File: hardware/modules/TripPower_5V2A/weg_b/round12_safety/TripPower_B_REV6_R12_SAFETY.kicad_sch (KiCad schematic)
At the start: 29 parts, among them Q301 MMBT3904LT1G, Q302 BSS138LT1G, Q401 TK11S10N1L,LQ, Q402 TK11S10N1L,LQ, Q403 BSS123LT1G, U301 TPS7A4001DGNR, U302 TMP390AQDRLRQ1, U303 TPS3838K33QDBVRQ1, U401 LTC4368HMS-2#WPBF

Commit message: fix(b): align isolated KiCad net labels and wires to placed component pin coordinates
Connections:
- net BASE_KILL: now also Q302.3 (D)
- net GND: now also U301.4 (GND), U301.9 (EP), U302.3 (GND), U303.2 (GND), U401.4 (RETRY), U401.5 (GND)
- net RAW_COMMON_SOURCE: now also Q401.3 (S), Q402.3 (S)
- net RAW_GATE: now also U401.10 (GATE)
- net RAW_LTC_SHDN: now also Q403.3 (D), U401.6 (SHDN)
- net RAW_OUT: now also U401.8 (VOUT)
- net RAW_OV: now also U401.3 (OV)
- net RAW_SENSE: now also U401.9 (SENSE)
- net RAW_UV: now also U401.2 (UV)
- net SAFE_3V3: now also U302.5 (VDD), U303.3 (MR), U303.5 (VDD)
- net SAFE_HV: now also U301.5 (EN), U301.8 (IN)
- net TEMP_OK_OD: now also U302.6 (OUTA)
- net TEMP_SET: now also U302.2 (SETB)
- net TPS_SHDN_SAFETY: now also Q301.3 (C)

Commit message: fix(b): place entire R12 schematic wire/pin geometry on KiCad 1.27mm connection grid and use TI EP footprint
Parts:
- U301: footprint Package_SO:MSOP-8-1EP_3x3mm_P0.65mm -> TripPower_B:TI_DGN0008B_HVSSOP_8_EP
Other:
- moved on the sheet: C301, C302, C303, C401, C402, D301, Q301, Q302, Q401, Q402, R301, R302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

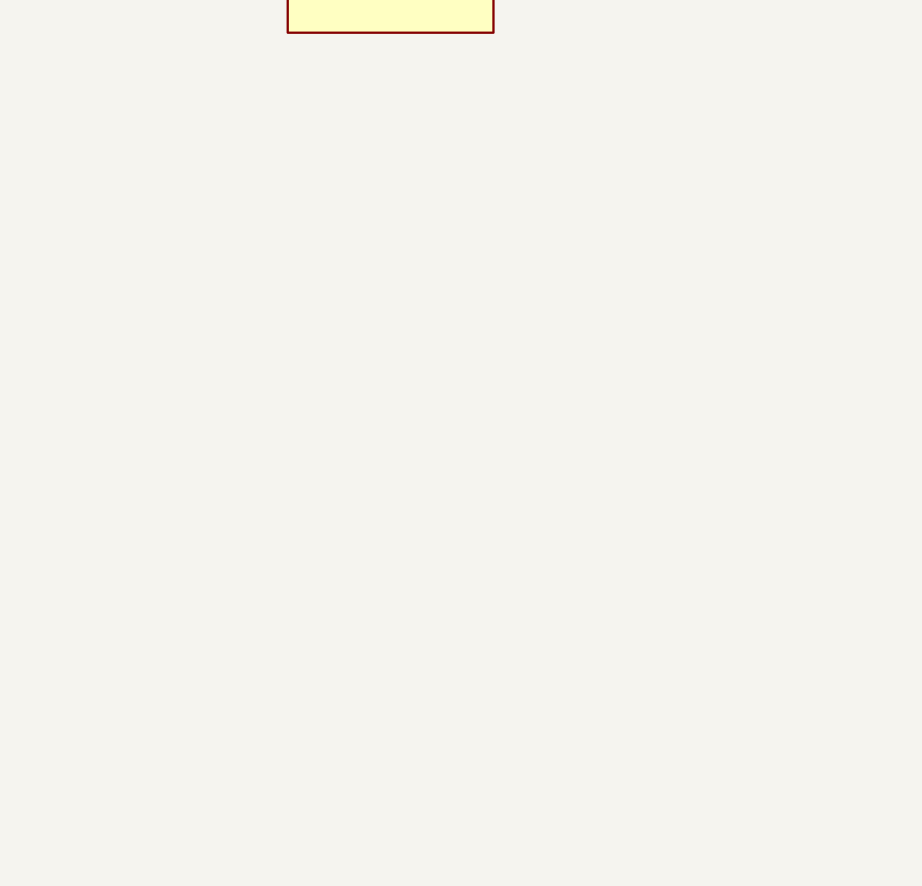
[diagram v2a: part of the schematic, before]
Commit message: fix(b): resolve two real ERC violations with GND supply flag and unfitted host interface; add mandatory RAW VOUT reservoir
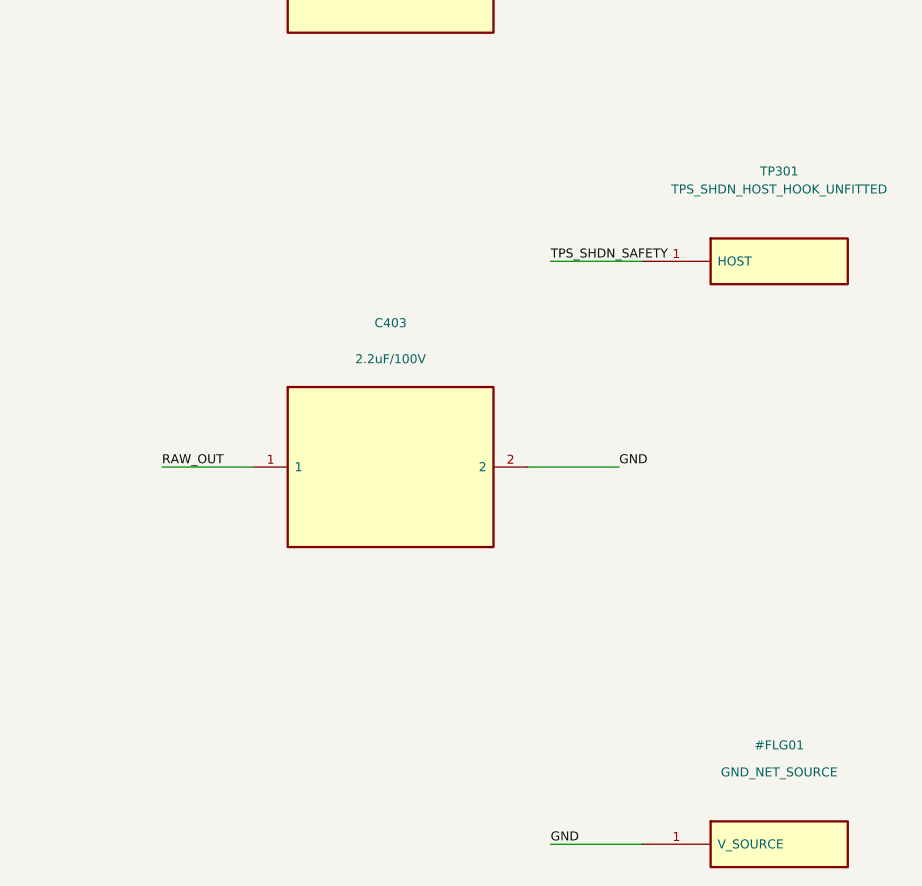
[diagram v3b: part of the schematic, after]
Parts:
- added C403: 2.2uF/100V, Capacitor_SMD:C_1210_3225Metric, symbol TripPower_B:CAP
- added TP301: TPS_SHDN_HOST_HOOK_UNFITTED, symbol TripPower_B:HOST_PORT
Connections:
- net GND: now also C403.2
- net RAW_OUT: now also C403.1
- net TPS_SHDN_SAFETY: now also TP301.1 (HOST)
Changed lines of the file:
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@@
 (no_connect (at 45.72 64.77))
 (no_connect (at 182.88 58.42))
+(symbol (lib_id "TripPower_B:CAP") (at 487.68 346.71 0) (unit 1) (in_bom yes) (on_board yes) (dnp no)
+(property "Reference" "C403" (at 487.68 330.71 0) (effects (font (size 1 1))))
+(property "Value" "2.2uF/100V" (at 487.68 334.71 0) (effects (font (size 1 1))))
+(property "MPN" "C1210C225K1RACAUTO" (at 487.68 346.71 0) (effects (font (size 1 1)) (hide yes)))
+(property "Manufacturer" "KEMET" (at 487.68 346.71 0) (effects (font (size 1 1)) (hide yes)))
+(property "Footprint" "Capacitor_SMD:C_1210_3225Metric" (at 487.68 346.71 0) (effects (font (size 1 1)) (hide yes)))
+(pin "1")
+(pin "2")
+(instances (project "TripPower_B_REV6_R12_SAFETY" (path "/10000000-0000-4000-8000-000000000001" (reference "C403") (unit 1)))))
+(symbol (lib_id "TripPower_B:POWER_FLAG") (at 530.86 388.62 0) (unit 1) (in_bom no) (on_board no) (dnp no)
+(property "Reference" "#FLG01" (at 530.86 377.62 0) (effects (font (size 1 1))))
+(property "Value" "GND_NET_SOURCE" (at 530.86 380.62 0) (effects (font (size 1 1))))
+(pin "1")
+(instances (project "TripPower_B_REV6_R12_SAFETY" (path "/10000000-0000-4000-8000-000000000001" (reference "#FLG01") (unit 1)))))
+(symbol (lib_id "TripPower_B:HOST_PORT") (at 530.86 323.85 0) (unit 1) (in_bom no) (on_board no) (dnp no)
+(property "Reference" "TP301" (at 530.86 313.85 0) (effects (font (size 1 1))))
+(property "Value" "TPS_SHDN_HOST_HOOK_UNFITTED" (at 530.86 315.85 0) (effects (font (size 1 1))))
+(pin "1")
+(instances (project "TripPower_B_REV6_R12_SAFETY" (path "/10000000-0000-4000-8000-000000000001" (reference "TP301") (unit 1)))))
+(wire (pts (xy 472.44 346.71) (xy 462.28 346.71)) (stroke (width 0) (type default)))
+(label "RAW_OUT" (at 462.28 346.71 180) (effects (font (size 1 1)) (justify left bottom)))
+(wire (pts (xy 502.92 346.71) (xy 513.08 346.71)) (stroke (width 0) (type default)))
+(label "GND" (at 513.08 346.71 0) (effects (font (size 1 1)) (justify left bottom)))
+(wire (pts (xy 515.62 388.62) (xy 505.46 388.62)) (stroke (width 0) (type default)))
+(label "GND" (at 505.46 388.62 180) (effects (font (size 1 1)) (justify left bottom)))
+(wire (pts (xy 515.62 323.85) (xy 505.46 323.85)) (stroke (width 0) (type default)))
+(label "TPS_SHDN_SAFETY" (at 505.46 323.85 180) (effects (font (size 1 1)) (justify left bottom)))
 )

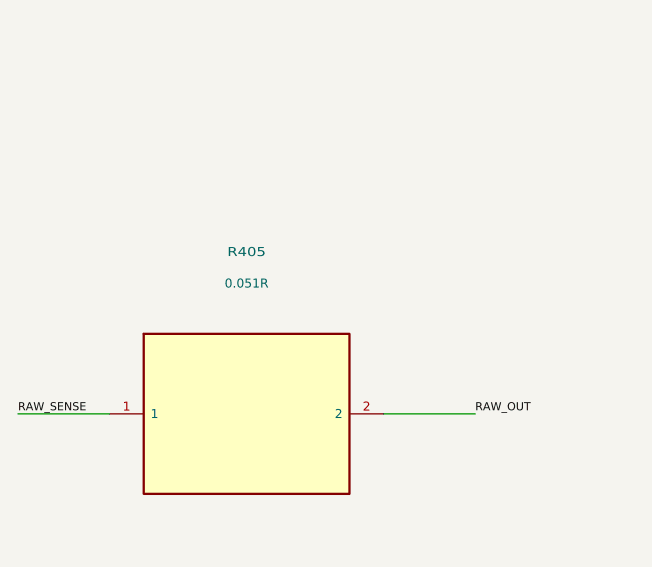
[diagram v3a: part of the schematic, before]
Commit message: fix(b): use real stocked AEC-Q200 Vishay 50mΩ 1% current-sense MPN with corrected min/max calculations
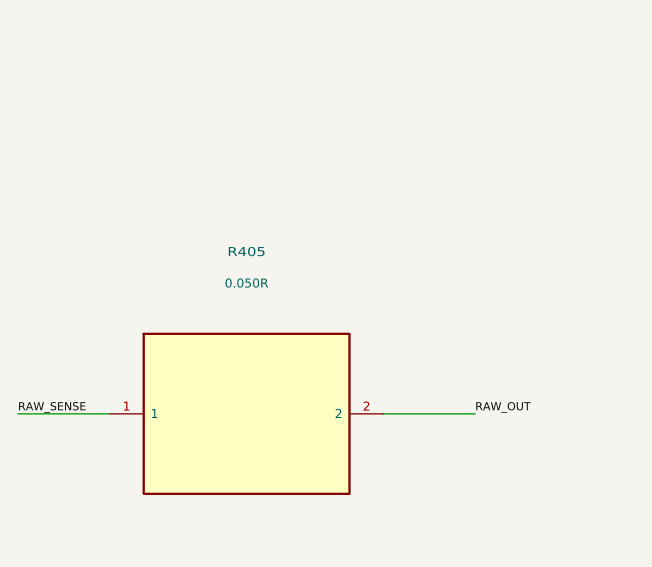
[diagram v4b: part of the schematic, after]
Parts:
- R405: value 0.051R -> 0.050R; MPN WSL2512R0510FEA -> WSL2512R0500FEA
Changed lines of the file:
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@@
 (symbol (lib_id "TripPower_B:RES") (at 60.96 289.56 0) (unit 1) (in_bom yes) (on_board yes) (dnp no)
  (property "Reference" "R405" (at 60.96 271.56 0) (effects (font (size 1 1.2))))
- (property "Value" "0.051R" (at 60.96 275.06 0) (effects (font (size 1 1))))
+ (property "Value" "0.050R" (at 60.96 275.06 0) (effects (font (size 1 1))))
  (property "Footprint" "Resistor_SMD:R_2512_6332Metric" (at 60.96 289.56 0) (effects (font (size 1 1)) (hide yes)))
- (property "MPN" "WSL2512R0510FEA" (at 60.96 289.56 0) (effects (font (size 1 1)) (hide yes)))
+ (property "MPN" "WSL2512R0500FEA" (at 60.96 289.56 0) (effects (font (size 1 1)) (hide yes)))
  (property "Manufacturer" "Vishay" (at 60.96 289.56 0) (effects (font (size 1 1)) (hide yes)))
  (pin "1")

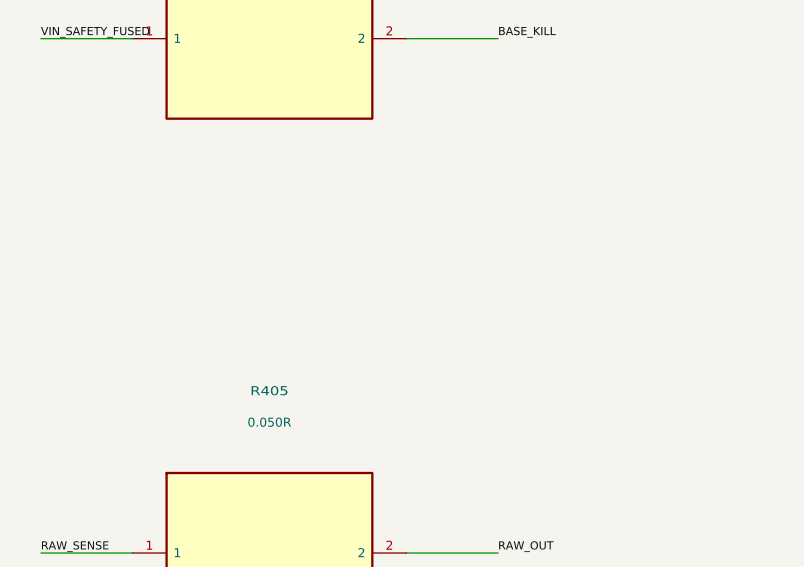
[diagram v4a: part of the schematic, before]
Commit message: safety(b): protect always-biased pre-Q201 NPN VBE against reverse-battery with reversible diode clamp
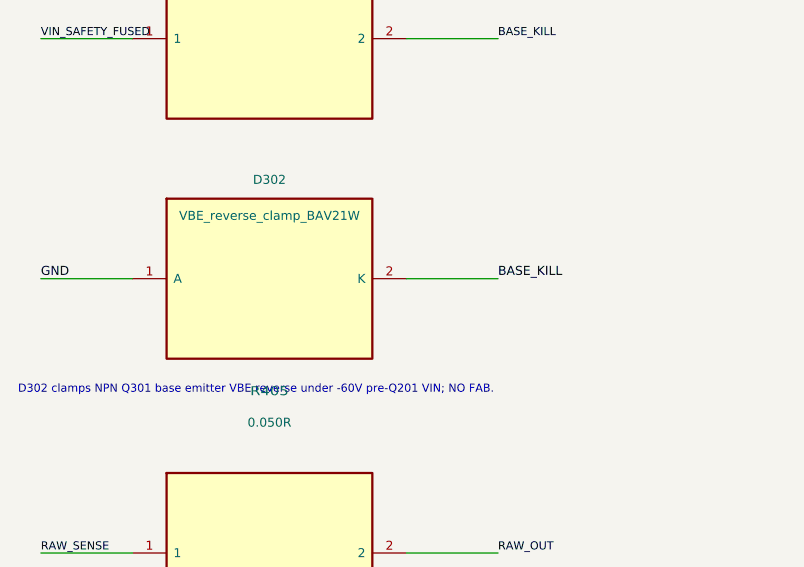
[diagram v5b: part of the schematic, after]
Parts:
- added D302: VBE_reverse_clamp_BAV21W, Diode_SMD:D_SOD-123, symbol TripPower_B:DIODE
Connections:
- net BASE_KILL: now also D302.2 (K)
- net GND: now also D302.1 (A)
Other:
- note added: "D302 clamps NPN Q301 base emitter VBE reverse under -60V pre-Q201 VIN; NO FAB."
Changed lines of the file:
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@@
 (wire (pts (xy 515.62 323.85) (xy 505.46 323.85)) (stroke (width 0) (type default)))
 (label "TPS_SHDN_SAFETY" (at 505.46 323.85 180) (effects (font (size 1 1)) (justify left bottom)))
+(text "D302 clamps NPN Q301 base emitter VBE reverse under -60V pre-Q201 VIN; NO FAB." (at 33.02 272 0) (effects (font (size 0.9 0.9)) (justify left bottom)))
+(symbol (lib_id "TripPower_B:DIODE") (at 60.96 259.08 0) (unit 1) (in_bom yes) (on_board yes) (dnp no)
+(property "Reference" "D302" (at 60.96 248.08 0) (effects (font (size 1 1))))
+(property "Value" "VBE_reverse_clamp_BAV21W" (at 60.96 252.08 0) (effects (font (size 1 1))))
+(property "MPN" "BAV21W-7-F" (at 60.96 259.08 0) (effects (font (size 1 1)) (hide yes)))
+(property "Manufacturer" "Diodes Incorporated" (at 60.96 259.08 0) (effects (font (size 1 1)) (hide yes)))
+(property "Footprint" "Diode_SMD:D_SOD-123" (at 60.96 259.08 0) (effects (font (size 1 1)) (hide yes)))
+(pin "1")
+(pin "2")
+(instances (project "TripPower_B_REV6_R12_SAFETY" (path "/10000000-0000-4000-8000-000000000001" (reference "D302") (unit 1)))))
+(wire (pts (xy 45.72 259.08) (xy 35.56 259.08)) (stroke (width 0) (type default)))
+(label "GND" (at 35.56 259.08 180) (effects (font (size 1 1)) (justify left bottom)))
+(wire (pts (xy 76.2 259.08) (xy 86.36 259.08)) (stroke (width 0) (type default)))
+(label "BASE_KILL" (at 86.36 259.08 0) (effects (font (size 1 1)) (justify left bottom)))
 )
